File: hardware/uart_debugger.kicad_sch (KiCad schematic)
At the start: 1 part, among them U3 UART_Module

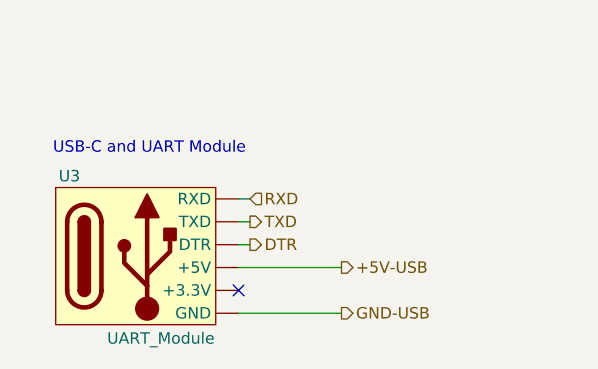
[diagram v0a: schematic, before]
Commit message: Added components to the UART Module to prevent backfeeding the module when the USB is not connected.
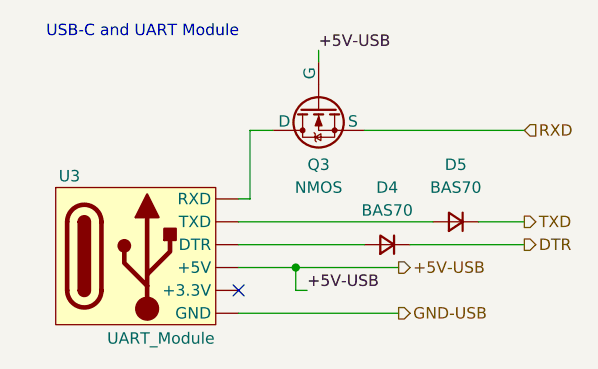
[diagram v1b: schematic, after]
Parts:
- added D4, D5: BAS70, symbol Device:D_Small
- added Q3: NMOS, symbol Simulation_SPICE:NMOS
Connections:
- net +5V-USB: now also Q3.2 (G)
- net DTR: now also D4.1 (K); no longer U3. (TXD)
- net RXD: now also Q3.3 (S); no longer U3. (TXD)
- net TXD: now also D5.1 (K); no longer U3. (TXD)
- new net: D4.2 (A), U3. (TXD)
- new net: Q3.1 (D), U3. (TXD)
- new net: D5.2 (A), U3. (TXD)

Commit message: Added some fields on the symbol table to record where to purchase components
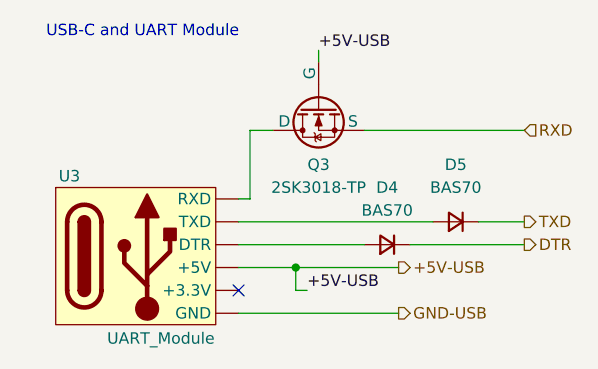
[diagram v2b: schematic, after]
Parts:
- D4, D5: Package (none) -> SOT-23-3; Part Num (none) -> BAS70-G; Price/unit (none) -> 1.09 kr; Supplier Link (none) -> https://www.mouser.se/ProductDetail/Comchip-Technology/BAS7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
- Q3: value NMOS -> 2SK3018-TP; Package (none) -> SOT-323-3; Part Num (none) -> 2SK3018-TP; Price/unit (none) -> 3,93 kr; Supplier Link (none) -> https://www.mouser.se/ProductDetail/Micro-Commercial-Compon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
- U3: Package (none) -> Module; Part Num (none) -> CH340E; Price/unit (none) -> 17,58kr; Supplier Link (none) -> https://es.aliexpress.com/item/1005004276046811.html?spm=a2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
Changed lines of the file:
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@@
 			)
 		)
-		(property "Datasheet" ""
+		(property "Datasheet" "https://cdn.sparkfun.com/assets/5/0/a/8/5/CH340DS1.PDF?utm_source=chatgpt.com"
 			(at 146.05 80.01 0)
 			(effects
@@
 			)
 		)
-		(property "Description" ""
+		(property "Description" "CH340E USB a TTL Module"
 			(at 146.05 80.01 0)
+			(effects
+				(font
+					(size 1.27 1.27)
+				)
+				(hide yes)
+			)
+		)
+		(property "Supplier Link" "https://es.aliexpress.com/item/1005004276046811.html?spm=a2g0o.order_list.order_list_main.39.6ba6194doVGuKx&gatewayAdapt=glo2esp"
+			(at 138.43 86.36 0)
+			(effects
+				(font
+					(size 1.27 1.27)
+				)
+				(hide yes)
+			)
+		)
+		(property "Price/unit" "17,58kr"
+			(at 138.43 86.36 0)
+			(effects
+				(font
+					(size 1.27 1.27)
+				)
+				(hide yes)
+			)
+		)
+		(property "Part Num" "CH340E"
+			(at 138.43 86.36 0)
+			(effects
+				(font
+					(size 1.27 1.27)
+				)
+				(hide yes)
+			)
+		)
+		(property "Package" "Module"
+			(at 138.43 86.36 0)
 			(effects
 				(font
@@
 			)
 		)
+		(property "Package" "SOT-23-3"
+			(at 165.1 85.09 0)
+			(effects
+				(font
+					(size 1.27 1.27)
+				)
+				(hide yes)
+			)
+		)
+		(property "Part Num" "BAS70-G"
+			(at 165.1 85.09 0)
+			(effects
+				(font
+					(size 1.27 1.27)
+				)
+				(hide yes)
+			)
+		)
+		(property "Price/unit" "1.09 kr"
+			(at 165.1 85.09 0)
+			(effects
+				(font
+					(size 1.27 1.27)
+				)
+				(hide yes)
+			)
+		)
+		(property "Supplier Link" "https://www.mouser.se/ProductDetail/Comchip-Technology/BAS70-G?qs=tw%252BuQ%2FB6PO1j2YRKFaqcxQ%3D%3D"
+			(at 165.1 85.09 0)
+			(effects
+				(font
+					(size 1.27 1.27)
+				)
+				(hide yes)
+			)
+		)
 		(pin "2"
 		)
@@
 			)
 		)
-		(property "Value" "NMOS"
+		(property "Value" "2SK3018-TP"
 			(at 157.48 78.74 90)
 			(effects
@@
 			)
 		)
-		(property "Datasheet" "https://ngspice.sourceforge.io/docs/ngspice-html-manual/manual.xhtml#cha_MOSFETs"
+		(property "Datasheet" "https://www.mouser.se/datasheet/2/258/2SK3018_SOT_323_-3364975.pdf"
 			(at 170.18 69.85 0)
 			(effects
@@
 			)
 		)
-		(property "Description" "N-MOSFET transistor, drain/source/gate"
+		(property "Description" "MOSFETs N-Channel MOSFET"
 			(at 157.48 69.85 0)
 			(effects
@@
 		(property "Sim.Pins" "1=D 2=G 3=S"
 			(at 172.72 69.85 0)
+			(effects
+				(font
+					(size 1.27 1.27)
+				)
+				(hide yes)
+			)
+		)
+		(property "Supplier Link" "https://www.mouser.se/ProductDetail/Micro-Commercial-Components-MCC/2SK3018-TP?qs=MoCBKJu1Jj0hqZl4P%2F2qSQ%3D%3D"
+			(at 157.48 69.85 0)
+			(effects
+				(font
+					(size 1.27 1.27)
+				)
+				(hide yes)
+			)
+		)
+		(property "Price/unit" "3,93 kr"
+			(at 157.48 69.85 0)
+			(effects
+				(font
+					(size 1.27 1.27)
+				)
+				(hide yes)
+			)
+		)
+		(property "Part Num" "2SK3018-TP"
+			(at 157.48 69.85 0)
+			(effects
+				(font
+					(size 1.27 1.27)
+				)
+				(hide yes)
+			)
+		)
+		(property "Package" "SOT-323-3"
+			(at 157.48 69.85 0)
 			(effects
 				(font
@@
 			(at 172.72 82.55 0)
 			(effects
+				(font
+					(size 1.27 1.27)
+				)
+				(hide yes)
+			)
+		)
+		(property "Supplier Link" "https://www.mouser.se/ProductDetail/Comchip-Technology/BAS70-G?qs=tw%252BuQ%2FB6PO1j2YRKFaqcxQ%3D%3D"
+			(at 172.72 82.55 0)
+			(effects
+				(font
+					(size 1.27 1.27)
+				)
+				(hide yes)
+			)
+		)
+		(property "Price/unit" "1.09 kr"
+			(at 172.72 82.55 0)
+			(effects
+				(font
+					(size 1.27 1.27)
+				)
+				(hide yes)
+			)
+		)
+		(property "Part Num" "BAS70-G"
+			(at 172.72 82.55 0)
+			(effects
+				(font
+					(size 1.27 1.27)
+				)
+				(hide yes)
+			)
+		)
+		(property "Package" "SOT-23-3"
+			(at 172.72 82.55 0)
+			(effects

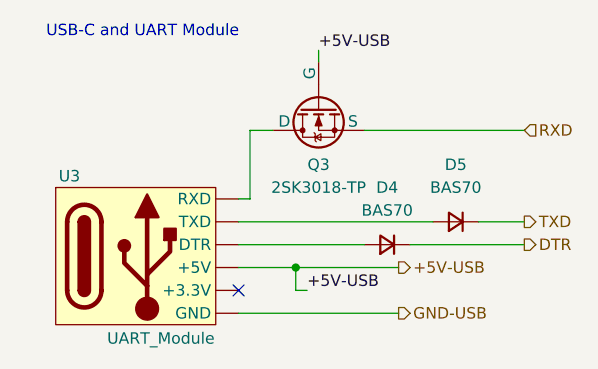
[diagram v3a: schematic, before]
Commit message: Added TP4056 footprint andconfirmed components in UART and BMS schematics.
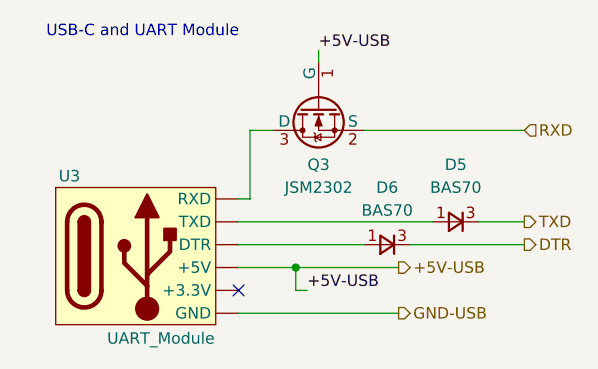
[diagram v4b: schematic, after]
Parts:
- removed D4: BAS70, symbol Device:D_Small
- added D6: BAS70, Package_TO_SOT_SMD:SOT-23, symbol Device:D_Small
- D5: footprint (none) -> Package_TO_SOT_SMD:SOT-23; Package SOT-23-3 -> SOT-23(TO-236); Part Num BAS70-G -> BAS70; Price/unit 1.09 kr -> $0.0189; Supplier Link https://www.mouser.se/ProductDetail/Comchip-Technology/BAS7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 -> https://jlcpcb.com/partdetail/Yangzhou_Yangjie_ElecTech-BAS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
- Q3: value 2SK3018-TP -> JSM2302; footprint (none) -> Package_TO_SOT_SMD:SOT-23; Package SOT-323-3 -> SOT-23; Part Num 2SK3018-TP -> JSM2302; Price/unit 3,93 kr -> $0.0201; Supplier Link https://www.mouser.se/ProductDetail/Micro-Commercial-Compon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 -> https://jlcpcb.com/partdetail/Jsmsemi-JSM2302/C916403
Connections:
- net +5V-USB: now also Q3.1 (G); no longer Q3.2 (G)
- net DTR: now also D6.3 (K)
- net RXD: now also Q3.2 (S); no longer Q3.3 (S)
- net TXD: now also D5.3 (K); no longer D5.1 (K)
- new net: D6.1 (A), U3. (TXD)
- new net: Q3.3 (D), U3. (TXD)
- new net: D5.1 (A), U3. (TXD)
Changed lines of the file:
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@@
+	)
+	(symbol
+		(lib_name "D_Small_1")
+		(lib_id "Device:D_Small")
+		(at 165.1 85.09 0)
+		(mirror y)
+		(unit 1)
+		(exclude_from_sim no)
+		(in_bom yes)
+		(on_board yes)
+		(dnp no)
+		(property "Reference" "D6"
+			(at 165.1 78.74 0)
+			(effects
+				(font
+					(size 1.27 1.27)
+				)
+			)
+		)
+		(property "Value" "BAS70"
+			(at 165.1 81.28 0)
+			(effects
+				(font
+					(size 1.27 1.27)
+				)
+			)
+		)
+		(property "Footprint" "Package_TO_SOT_SMD:SOT-23"
+			(at 144.018 85.344 90)
+			(effects
+				(font
+					(size 1.27 1.27)
+				)
+				(hide yes)
+			)
+		)
+		(property "Datasheet" "https://wmsc.lcsc.com/wmsc/upload/file/pdf/v2/lcsc/2201131400_Yangzhou-Yangjie-Elec-Tech-BAS70_C968045.pdf"
+			(at 147.828 84.328 90)
+			(effects
+				(font
+					(size 1.27 1.27)
+				)
+				(hide yes)
+			)
+		)
+		(property "Description" "70V Independent Type 1V@15mA 70mA SOT-23(TO-236) Schottky Diodes ROHS"
+			(at 163.83 66.548 0)
+			(effects
+				(font
+					(size 1.27 1.27)
+				)
+				(hide yes)
+			)
+		)
+		(property "Sim.Device" "D"
+			(at 172.974 80.518 0)
+			(effects
+				(font
+					(size 1.27 1.27)
+				)
+				(hide yes)
+			)
+		)
+		(property "Sim.Pins" "1=K 2=A"
+			(at 153.924 74.422 0)
+			(effects
+				(font
+					(size 1.27 1.27)
+				)
+				(hide yes)
+			)
+		)
+		(property "Supplier Link" "https://jlcpcb.com/partdetail/Yangzhou_Yangjie_ElecTech-BAS70/C968045"
+			(at 161.29 64.008 0)
+			(effects
+				(font
+					(size 1.27 1.27)
+				)
+				(hide yes)
+			)
+		)
+		(property "Price/unit" "$0.0189"
+			(at 164.846 73.66 0)
+			(effects
+				(font
+					(size 1.27 1.27)
+				)
+				(hide yes)
+			)
+		)
+		(property "Part Num" "BAS70"
+			(at 134.366 73.152 0)
+			(effects
+				(font
+					(size 1.27 1.27)
+				)
+				(hide yes)
+			)
+		)
+		(property "Package" "SOT-23(TO-236)"
+			(at 163.576 70.104 0)
+			(effects
+				(font
+					(size 1.27 1.27)
+				)
+				(hide yes)
+			)
+		)
+		(pin "3"
+		)
+		(pin "1"
+		)
+		(instances
+			(project "kitchen_timer-hardware"
+				(path "/8963deea-96bc-4401-b671-98fbe9ed9c6a/f7e640d9-c0d9-4c44-8592-f18e152ed7d5"
+					(reference "D6")
+					(unit 1)
+				)
+			)
+		)
 	)
 	(symbol
@@
 				(path "/8963deea-96bc-4401-b671-98fbe9ed9c6a/f7e640d9-c0d9-4c44-8592-f18e152ed7d5"
 					(reference "U3")
-					(unit 1)
-				)
-			)
-		)
-	)
-	(symbol
-		(lib_id "Device:D_Small")
-		(at 165.1 85.09 0)
-		(mirror y)
-		(unit 1)
-		(exclude_from_sim no)
-		(in_bom yes)
-		(on_board yes)
-		(dnp no)
-		(property "Reference" "D4"
-			(at 165.1 78.74 0)
-			(effects
-				(font
-					(size 1.27 1.27)
-				)
-			)
-		)
-		(property "Value" "BAS70"
-			(at 165.1 81.28 0)
-			(effects
-				(font
-					(size 1.27 1.27)
-				)
-			)
-		)
-		(property "Footprint" ""
-			(at 165.1 85.09 90)
-			(effects
-				(font
-					(size 1.27 1.27)
-				)
-				(hide yes)
-			)
-		)
-		(property "Datasheet" "https://www.mouser.se/datasheet/2/80/datasheet-BAS70-1160237.pdf"
-			(at 165.1 85.09 90)
-			(effects
-				(font
-					(size 1.27 1.27)
-				)
-				(hide yes)
-			)
-		)
-		(property "Description" "Diode, small symbol"
-			(at 165.1 85.09 0)
-			(effects
-				(font
-					(size 1.27 1.27)
-				)
-				(hide yes)
-			)
-		)
-		(property "Sim.Device" "D"
-			(at 165.1 85.09 0)
-			(effects
-				(font
-					(size 1.27 1.27)
-				)
-				(hide yes)
-			)
-		)
-		(property "Sim.Pins" "1=K 2=A"
-			(at 165.1 85.09 0)
-			(effects
-				(font
-					(size 1.27 1.27)
-				)
-				(hide yes)
-			)
-		)
-		(property "Package" "SOT-23-3"
-			(at 165.1 85.09 0)
-			(effects
-				(font
-					(size 1.27 1.27)
-				)
-				(hide yes)
-			)
-		)
-		(property "Part Num" "BAS70-G"
-			(at 165.1 85.09 0)
-			(effects
-				(font
-					(size 1.27 1.27)
-				)
-				(hide yes)
-			)
-		)
-		(property "Price/unit" "1.09 kr"
-			(at 165.1 85.09 0)
-			(effects
-				(font
-					(size 1.27 1.27)
-				)
-				(hide yes)
-			)
-		)
-		(property "Supplier Link" "https://www.mouser.se/ProductDetail/Comchip-Technology/BAS70-G?qs=tw%252BuQ%2FB6PO1j2YRKFaqcxQ%3D%3D"
-			(at 165.1 85.09 0)
-			(effects
-				(font
-					(size 1.27 1.27)
-				)
-				(hide yes)
-			)
-		)
-		(pin "2"
-		)
-		(pin "1"
-		)
-		(instances
-			(project ""
-				(path "/8963deea-96bc-4401-b671-98fbe9ed9c6a/f7e640d9-c0d9-4c44-8592-f18e152ed7d5"
-					(reference "D4")
 					(unit 1)
 				)
@@
 			)
 		)
-		(property "Value" "2SK3018-TP"
+		(property "Value" "JSM2302"
 			(at 157.48 78.74 90)
 			(effects
@@
 			)
 		)
-		(property "Footprint" ""
+		(property "Footprint" "Package_TO_SOT_SMD:SOT-23"
 			(at 154.94 74.93 0)
 			(effects
@@
 			)
 		)
-		(property "Datasheet" "https://www.mouser.se/datasheet/2/258/2SK3018_SOT_323_-3364975.pdf"
+		(property "Datasheet" "https://www.lcsc.com/datasheet/lcsc_datasheet_2308071512_JSMSEMI-JSM2302_C916403.pdf"
 			(at 170.18 69.85 0)
 			(effects
@@
 			)
 		)
-		(property "Description" "MOSFETs N-Channel MOSFET"
+		(property "Description" "20V 6A 26mΩ@4.5V,6A 1.25W 1.2V@250uA 1 N-Channel SOT-23 MOSFETs ROHS"
 			(at 157.48 69.85 0)
 			(effects
@@
 			)
 		)
-		(property "Supplier Link" "https://www.mouser.se/ProductDetail/Micro-Commercial-Components-MCC/2SK3018-TP?qs=MoCBKJu1Jj0hqZl4P%2F2qSQ%3D%3D"
+		(property "Supplier Link" "https://jlcpcb.com/partdetail/Jsmsemi-JSM2302/C916403"
 			(at 157.48 69.85 0)
 			(effects
@@
 			)
 		)
-		(property "Price/unit" "3,93 kr"
+		(property "Price/unit" "$0.0201"
 			(at 157.48 69.85 0)
 			(effects
@@
 			)
 		)
-		(property "Part Num" "2SK3018-TP"
+		(property "Part Num" "JSM2302"
 			(at 157.48 69.85 0)
 			(effects
@@
 			)
 		)
-		(property "Package" "SOT-323-3"
+		(property "Package" "SOT-23"
 			(at 157.48 69.85 0)
 			(effects
@@
 	)
 	(symbol
+		(lib_name "D_Small_1")
 		(lib_id "Device:D_Small")
 		(at 172.72 82.55 0)
@@
 			)
 		)
-		(property "Footprint" ""
-			(at 172.72 82.55 90)
-			(effects
-				(font
-					(size 1.27 1.27)
-				)
-				(hide yes)
-			)
-		)
-		(property "Datasheet" "https://www.mouser.se/datasheet/2/80/datasheet-BAS70-1160237.pdf"
-			(at 172.72 82.55 90)
-			(effects
-				(font
-					(size 1.27 1.27)
-				)
-				(hide yes)
-			)
-		)
-		(property "Description" "Diode, small symbol"
-			(at 172.72 82.55 0)
+		(property "Footprint" "Package_TO_SOT_SMD:SOT-23"
+			(at 151.638 82.804 90)
+			(effects
+				(font
+					(size 1.27 1.27)
+				)
+				(hide yes)
+			)
+		)
+		(property "Datasheet" "https://wmsc.lcsc.com/wmsc/upload/file/pdf/v2/lcsc/2201131400_Yangzhou-Yangjie-Elec-Tech-BAS70_C968045.pdf"
+			(at 155.448 81.788 90)
+			(effects
+				(font
+					(size 1.27 1.27)
+				)
+				(hide yes)
+			)
+		)
+		(property "Description" "70V Independent Type 1V@15mA 70mA SOT-23(TO-236) Schottky Diodes ROHS"
+			(at 171.45 64.008 0)
 			(effects
 				(font
@@
 		)
 		(property "Sim.Device" "D"
-			(at 172.72 82.55 0)
+			(at 180.594 77.978 0)
 			(effects
 				(font
@@
 		)
 		(property "Sim.Pins" "1=K 2=A"
-			(at 172.72 82.55 0)
-			(effects
-				(font
-					(size 1.27 1.27)
-				)
-				(hide yes)
-			)
-		)
-		(property "Supplier Link" "https://www.mouser.se/ProductDetail/Comchip-Technology/BAS70-G?qs=tw%252BuQ%2FB6PO1j2YRKFaqcxQ%3D%3D"
-			(at 172.72 82.55 0)
-			(effects
-				(font
-					(size 1.27 1.27)
-				)
-				(hide yes)
-			)
-		)
-		(property "Price/unit" "1.09 kr"
-			(at 172.72 82.55 0)
-			(effects
-				(font
-					(size 1.27 1.27)
-				)
-				(hide yes)
-			)
-		)
-		(property "Part Num" "BAS70-G"
-			(at 172.72 82.55 0)
-			(effects
-				(font
-					(size 1.27 1.27)
-				)
-				(hide yes)
-			)
-		)
-		(property "Package" "SOT-23-3"
-			(at 172.72 82.55 0)
-			(effects
-				(font
-					(size 1.27 1.27)
-				)
-				(hide yes)
-			)
-		)
-		(pin "2"
+			(at 161.544 71.882 0)
+			(effects
+				(font
+					(size 1.27 1.27)
+				)
+				(hide yes)
+			)
+		)
+		(property "Supplier Link" "https://jlcpcb.com/partdetail/Yangzhou_Yangjie_ElecTech-BAS70/C968045"
+			(at 168.91 61.468 0)
+			(effects
+				(font
+					(size 1.27 1.27)
+				)
+				(hide yes)
+			)
+		)
+		(property "Price/unit" "$0.0189"
+			(at 172.466 71.12 0)
+			(effects
+				(font
+					(size 1.27 1.27)
+				)
+				(hide yes)
+			)
+		)
+		(property "Part Num" "BAS70"
+			(at 141.986 70.612 0)
+			(effects
+				(font
+					(size 1.27 1.27)
+				)
+				(hide yes)
+			)
+		)
+		(property "Package" "SOT-23(TO-236)"
+			(at 171.196 67.564 0)
+			(effects
+				(font
+					(size 1.27 1.27)
+				)
+				(hide yes)
+			)
+		)
+		(pin "3"
 		)
 		(pin "1"

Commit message: Removed the 3.3V Regulator since we might need to run everything out of 5V
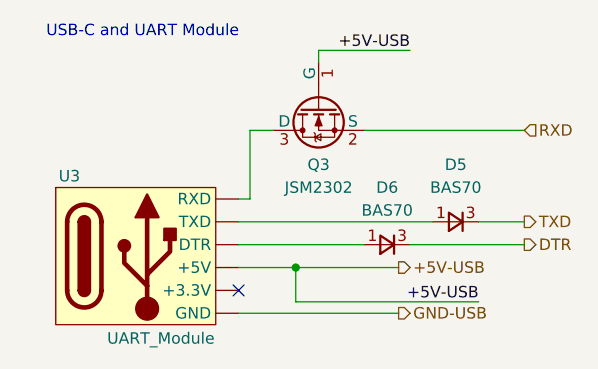
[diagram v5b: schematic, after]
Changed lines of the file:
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@@
 	(wire
 		(pts
-			(xy 154.94 87.63) (xy 154.94 90.17)
+			(xy 154.94 87.63) (xy 154.94 91.44)
 		)
 		(stroke
@@
 	(wire
 		(pts
+			(xy 157.48 63.5) (xy 157.48 64.77)
+		)
+		(stroke
+			(width 0)
+			(type default)
+		)
+	)
+	(wire
+		(pts
 			(xy 148.59 87.63) (xy 154.94 87.63)
 		)
@@
 	(wire
 		(pts
-			(xy 157.48 63.5) (xy 157.48 64.77)
+			(xy 167.64 63.5) (xy 157.48 63.5)
 		)
 		(stroke
@@
 	(wire
 		(pts
-			(xy 154.94 90.17) (xy 156.21 90.17)
+			(xy 154.94 91.44) (xy 175.26 91.44)
 		)
 		(stroke
@@
 	)
 	(label "+5V-USB"
-		(at 156.21 90.17 0)
+		(at 175.26 91.44 180)
 		(fields_autoplaced yes)
 		(effects
@@
 				(size 1.27 1.27)
 			)
-			(justify left bottom)
+			(justify right bottom)
 		)
 	)
 	(label "+5V-USB"
-		(at 157.48 63.5 0)
+		(at 167.64 63.5 180)
 		(fields_autoplaced yes)
 		(effects
@@
 				(size 1.27 1.27)
 			)
-			(justify left bottom)
+			(justify right bottom)
 		)
 	)

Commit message: stuff. At this point we decided it is not worth tracking changes on schematics
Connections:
- net RXD: now also Q3.3 (D); no longer Q3.2 (S)
- new net: Q3.2 (S), U3. (GND)
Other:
- moved on the sheet: Q3
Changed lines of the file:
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@@
 (kicad_sch
-	(version 20231120)
+	(version 20250114)
 	(generator "eeschema")
-	(generator_version "8.0")
+	(generator_version "9.0")
 	(paper "A4")
 	(title_block
@@
 		(comment 4 "Author: Nicolas Perozzi")
 	)
+	(text "USB-C and UART Module"
+		(exclude_from_sim no)
+		(at 137.922 61.468 0)
+		(effects
+			(font
+				(size 1.27 1.27)
+			)
+		)
+	)
 	(junction
 		(at 154.94 87.63)
@@
 		)
 	)
-	(text "USB-C and UART Module"
-		(exclude_from_sim no)
-		(at 137.922 61.468 0)
-		(effects
-			(font
-				(size 1.27 1.27)
-			)
-		)
-	)
 	(label "+5V-USB"
 		(at 175.26 91.44 180)
-		(fields_autoplaced yes)
 		(effects
 			(font
@@
 	(label "+5V-USB"
 		(at 167.64 63.5 180)
-		(fields_autoplaced yes)
 		(effects
 			(font
@@
 		(shape input)
 		(at 180.34 72.39 0)
-		(fields_autoplaced yes)
 		(effects
 			(font
@@
 		(shape output)
 		(at 180.34 85.09 0)
-		(fields_autoplaced yes)
 		(effects
 			(font
@@
 		(shape output)
 		(at 166.37 87.63 0)
-		(fields_autoplaced yes)
 		(effects
 			(font
@@
 		(shape output)
 		(at 166.37 92.71 0)
-		(fields_autoplaced yes)
 		(effects
 			(font
@@
 		(shape output)
 		(at 180.34 82.55 0)
-		(fields_autoplaced yes)
 		(effects
 			(font
@@
 	(symbol
 		(lib_id "Simulation_SPICE:NMOS")
-		(at 157.48 69.85 90)
-		(mirror x)
+		(at 157.48 69.85 270)
 		(unit 1)
 		(exclude_from_sim no)
@@
 		)
 		(property "Footprint" "Package_TO_SOT_SMD:SOT-23"
-			(at 154.94 74.93 0)
+			(at 160.02 74.93 0)
 			(effects
 				(font
@@
 		)
 		(property "Datasheet" "https://www.lcsc.com/datasheet/lcsc_datasheet_2308071512_JSMSEMI-JSM2302_C916403.pdf"
-			(at 170.18 69.85 0)
+			(at 144.78 69.85 0)
 			(effects
 				(font
@@
 		)
 		(property "Sim.Device" "NMOS"
-			(at 174.625 69.85 0)
+			(at 140.335 69.85 0)
 			(effects
 				(font
@@
 		)
 		(property "Sim.Type" "VDMOS"
-			(at 176.53 69.85 0)
+			(at 138.43 69.85 0)
 			(effects
 				(font
@@
 		)
 		(property "Sim.Pins" "1=D 2=G 3=S"
-			(at 172.72 69.85 0)
-			(effects
-				(font
+			(at 142.24 69.85 0)
+			(effects
+				(font
